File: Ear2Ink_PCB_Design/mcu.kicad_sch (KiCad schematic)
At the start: 43 parts, among them J1 Conn_01x16_Pin, J2 Conn_01x08_Pin, J3 Conn_01x08_Pin, J4 MEM2052-00-195-00-A_REVA, J5 Conn_01x06_Pin, J6 Conn_01x04_Pin, J7 Conn_01x03_Pin, J8 Conn_01x16_Pin, SW1 SW_Push, U1 STM32F411RETx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

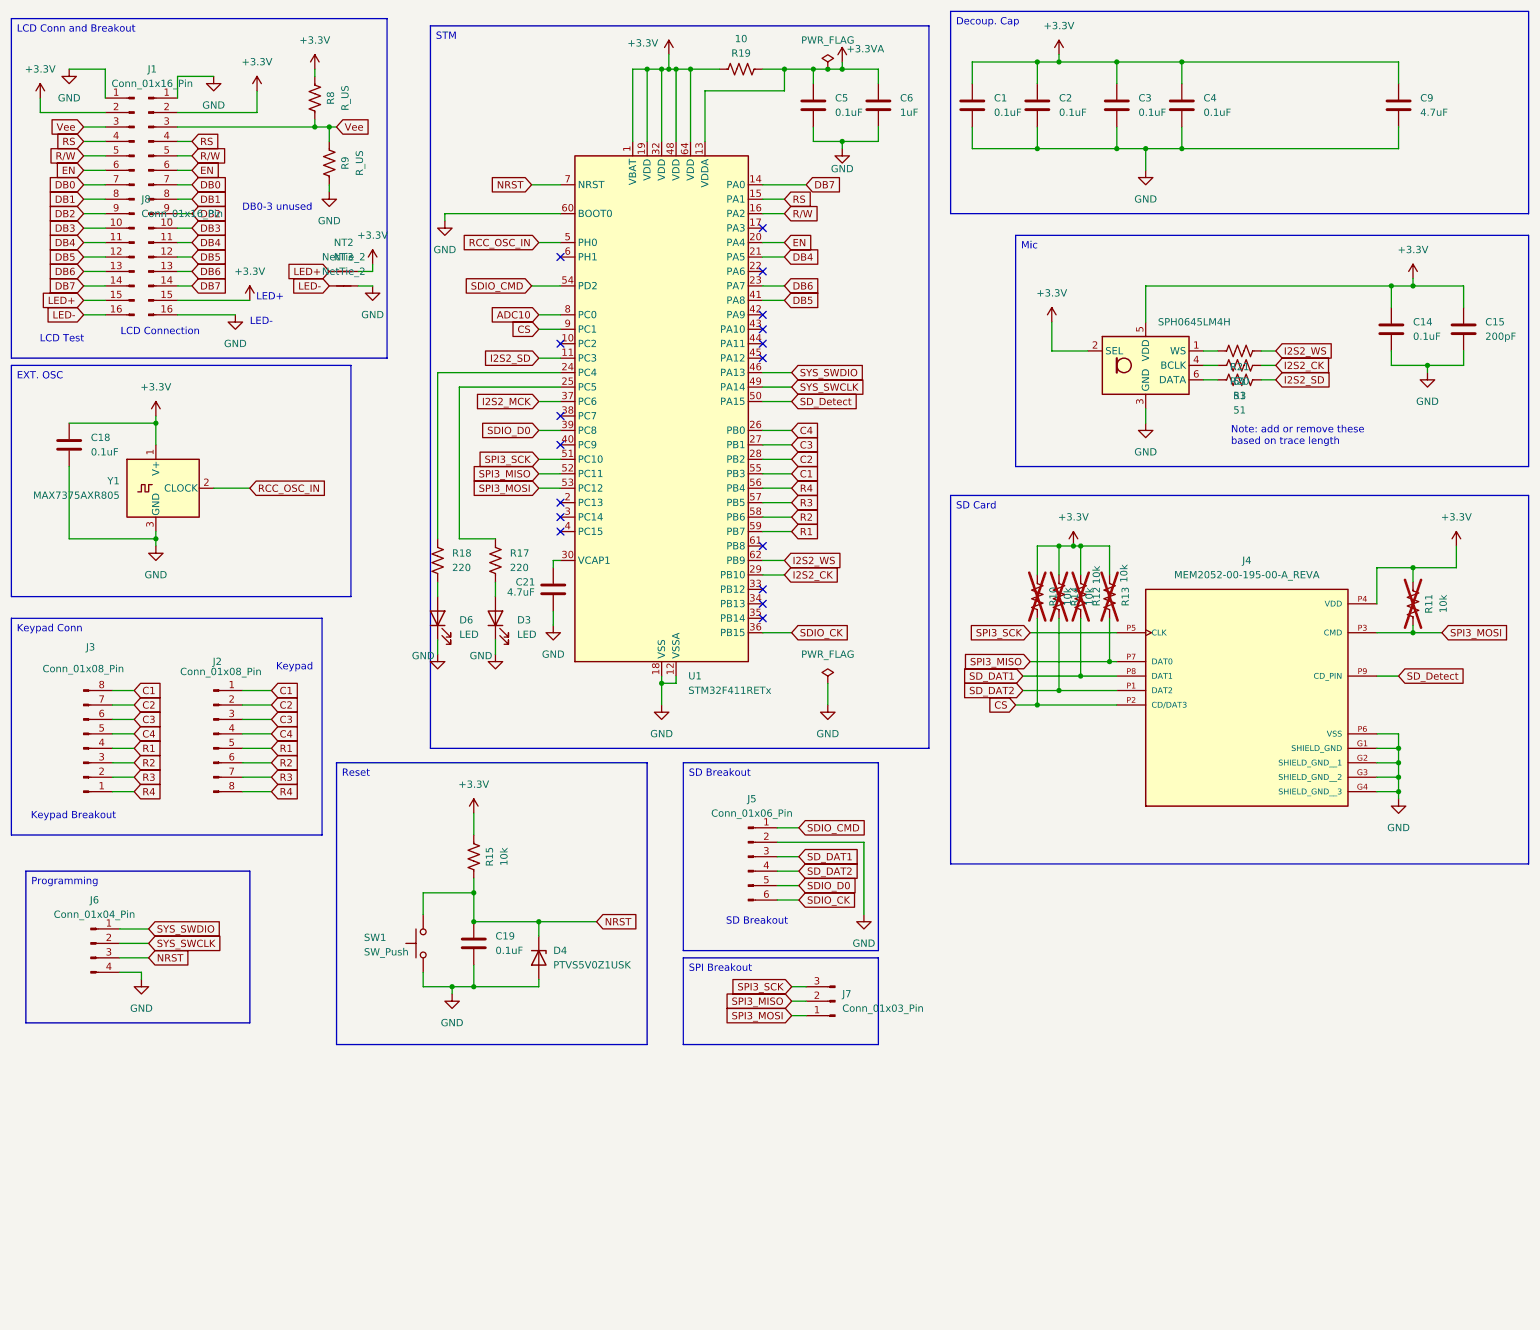
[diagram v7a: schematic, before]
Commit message: New Parts Added
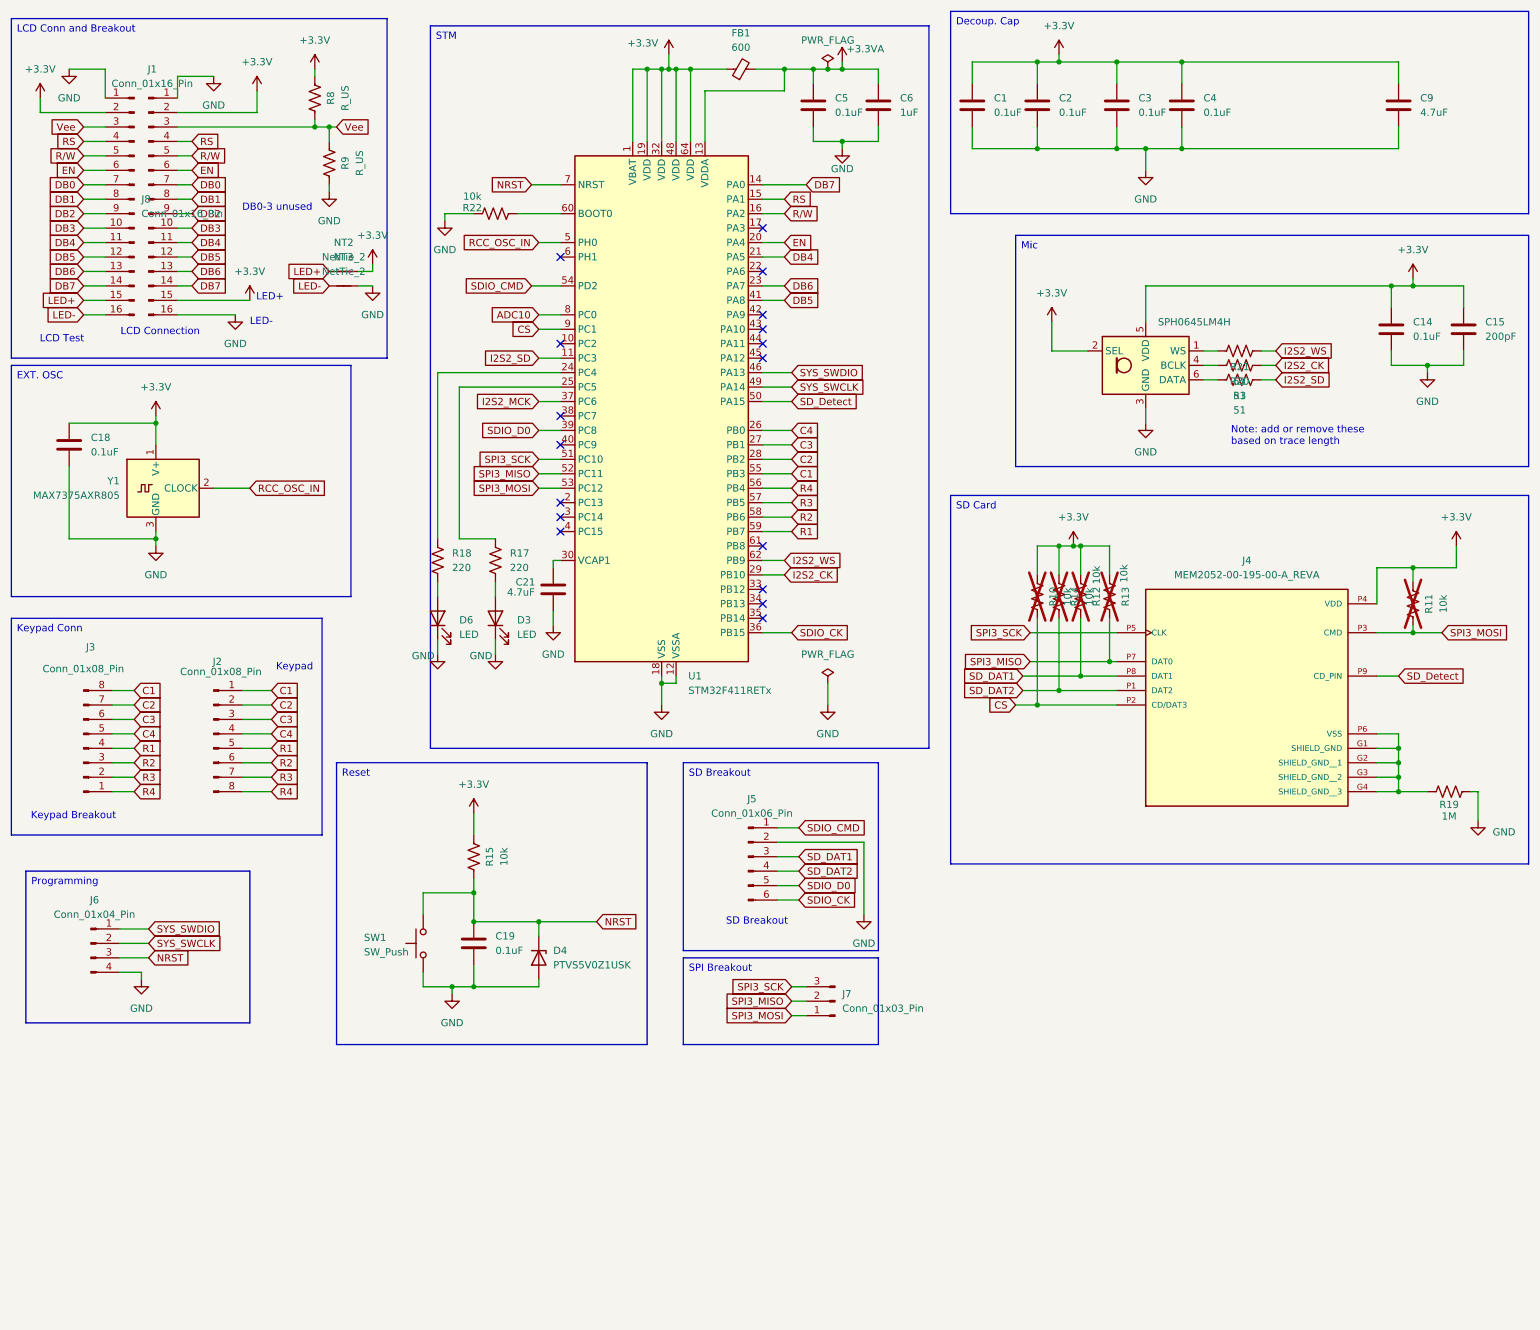
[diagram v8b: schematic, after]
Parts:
- added FB1: 600, symbol Device:FerriteBead_Small
- added R22: 10k, Resistor_SMD:R_0603_1608Metric_Pad0.98x0.95mm_HandSolder, symbol Device:R_US
- R19: value 10 -> 1M
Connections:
- net +3.3V: now also FB1.1; no longer R19.1
- net +3.3VA: now also FB1.2; no longer R19.2
- net GND: now also R19.1, R22.1; no longer J4.G1 (SHIELD_GND), J4.G2 (SHIELD_GND__1), J4.G3 (SHIELD_GND__2), J4.G4 (SHIELD_GND__3), J4.P6 (VSS), U1.60 (BOOT0)
- new net: R22.2, U1.60 (BOOT0)
- new net: J4.G1 (SHIELD_GND), J4.G2 (SHIELD_GND__1), J4.G3 (SHIELD_GND__2), J4.G4 (SHIELD_GND__3), J4.P6 (VSS), R19.2
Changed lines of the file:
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@@
 	)
 	(junction
-		(at 260.35 151.13)
-		(diameter 0)
-		(color 0 0 0 0)
-	)
-	(junction
 		(at 97.79 173.99)
 		(diameter 0)
@@
 	)
 	(junction
+		(at 260.35 151.13)
+		(diameter 0)
+		(color 0 0 0 0)
+	)
+	(junction
 		(at 157.48 24.13)
 		(diameter 0)
@@
 	(wire
 		(pts
+			(xy 260.35 151.13) (xy 265.43 151.13)
+		)
+		(stroke
+			(width 0)
+			(type default)
+		)
+	)
+	(wire
+		(pts
 			(xy 34.29 148.59) (xy 38.1 148.59)
 		)
@@
 	(wire
 		(pts
+			(xy 105.41 49.53) (xy 113.03 49.53)
+		)
+		(stroke
+			(width 0)
+			(type default)
+		)
+	)
+	(wire
+		(pts
 			(xy 152.4 24.13) (xy 157.48 24.13)
 		)
@@
 	(wire
 		(pts
-			(xy 113.03 49.53) (xy 92.71 49.53)
-		)
-		(stroke
-			(width 0)
-			(type default)
-		)
-	)
-	(wire
-		(pts
 			(xy 91.44 114.3) (xy 91.44 116.84)
 		)
@@
 	(wire
 		(pts
-			(xy 148.59 24.13) (xy 152.4 24.13)
-		)
-		(stroke
-			(width 0)
-			(type default)
-		)
-	)
-	(wire
-		(pts
 			(xy 35.56 175.26) (xy 40.64 175.26)
 		)
@@
 	(wire
 		(pts
+			(xy 147.32 24.13) (xy 152.4 24.13)
+		)
+		(stroke
+			(width 0)
+			(type default)
+		)
+	)
+	(wire
+		(pts
 			(xy 109.22 92.71) (xy 113.03 92.71)
 		)
@@
 	(wire
 		(pts
+			(xy 274.32 151.13) (xy 274.32 156.21)
+		)
+		(stroke
+			(width 0)
+			(type default)
+		)
+	)
+	(wire
+		(pts
 			(xy 59.69 27.94) (xy 59.69 31.75)
 		)
@@
 	(wire
 		(pts
-			(xy 260.35 151.13) (xy 260.35 152.4)
+			(xy 273.05 151.13) (xy 274.32 151.13)
 		)
 		(stroke
@@
 	(wire
 		(pts
-			(xy 135.89 24.13) (xy 140.97 24.13)
+			(xy 135.89 24.13) (xy 142.24 24.13)
 		)
 		(stroke
@@
 	(wire
 		(pts
+			(xy 92.71 49.53) (xy 97.79 49.53)
+		)
+		(stroke
+			(width 0)
+			(type default)
+		)
+	)
+	(wire
+		(pts
 			(xy 69.85 33.02) (xy 69.85 34.29)
 		)
@@
 	(symbol
 		(lib_id "Device:R_US")
+		(at 101.6 49.53 90)
+		(unit 1)
+		(exclude_from_sim no)
+		(in_bom yes)
+		(on_board yes)
+		(dnp no)
+		(property "Reference" "R22"
+			(at 97.536 48.514 90)
+			(effects
+				(font
+					(size 1.27 1.27)
+				)
+			)
+		)
+		(property "Value" "10k"
+			(at 97.536 46.482 90)
+			(effects
+				(font
+					(size 1.27 1.27)
+				)
+			)
+		)
+		(property "Footprint" "Resistor_SMD:R_0603_1608Metric_Pad0.98x0.95mm_HandSolder"
+			(at 101.854 48.514 90)
+			(effects
+				(font
+					(size 1.27 1.27)
+				)
+				(hide yes)
+			)
+		)
+		(property "Datasheet" "~"
+			(at 101.6 49.53 0)
+			(effects
+				(font
+					(size 1.27 1.27)
+				)
+				(hide yes)
+			)
+		)
+		(property "Description" "Resistor, US symbol"
+			(at 101.6 49.53 0)
+			(effects
+				(font
+					(size 1.27 1.27)
+				)
+				(hide yes)
+			)
+		)
+		(pin "2"
+		)
+		(pin "1"
+		)
+		(instances
+			(project "Ear2Ink_PCB_Design"
+				(path "/cdb6d8ac-bdfd-4608-bf70-aa82e76498ad/2ddad00a-af62-4659-9017-a3cd158a818d"
+					(reference "R22")
+					(unit 1)
+				)
+			)
+		)
+	)
+	(symbol
+		(lib_id "Device:R_US")
 		(at 232.41 78.74 270)
 		(unit 1)
@@
 	)
 	(symbol
-		(lib_id "Device:R_US")
-		(at 144.78 24.13 90)
-		(unit 1)
-		(exclude_from_sim no)
-		(in_bom yes)
-		(on_board yes)
-		(dnp no)
-		(property "Reference" "R19"
-			(at 144.78 21.336 90)
-			(effects
-				(font
-					(size 1.27 1.27)
-				)
-			)
-		)
-		(property "Value" "10"
-			(at 144.78 18.796 90)
-			(effects
-				(font
-					(size 1.27 1.27)
-				)
-			)
-		)
-		(property "Footprint" "Resistor_SMD:R_0603_1608Metric_Pad0.98x0.95mm_HandSolder"
-			(at 145.034 23.114 90)
-			(effects
-				(font
-					(size 1.27 1.27)
-				)
-				(hide yes)
-			)
-		)
-		(property "Datasheet" "~"
-			(at 144.78 24.13 0)
-			(effects
-				(font
-					(size 1.27 1.27)
-				)
-				(hide yes)
-			)
-		)
-		(property "Description" "Resistor, US symbol"
-			(at 144.78 24.13 0)
-			(effects
-				(font
-					(size 1.27 1.27)
-				)
-				(hide yes)
-			)
-		)
-		(pin "2"
-		)
-		(pin "1"
-		)
-		(instances
-			(project "Ear2Ink_PCB_Design"
-				(path "/cdb6d8ac-bdfd-4608-bf70-aa82e76498ad/2ddad00a-af62-4659-9017-a3cd158a818d"
-					(reference "R19")
-					(unit 1)
-				)
-			)
-		)
-	)
-	(symbol
 		(lib_id "Device:NetTie_2")
 		(at 74.93 59.69 0)
@@
 	)
 	(symbol
+		(lib_id "Device:FerriteBead_Small")
+		(at 144.78 24.13 90)
+		(unit 1)
+		(exclude_from_sim no)
+		(in_bom yes)
+		(on_board yes)
+		(dnp no)
+		(fields_autoplaced yes)
+		(property "Reference" "FB1"
+			(at 144.7419 17.78 90)
+			(effects
+				(font
+					(size 1.27 1.27)
+				)
+			)
+		)
+		(property "Value" "600"
+			(at 144.7419 20.32 90)
+			(effects
+				(font
+					(size 1.27 1.27)
+				)
+			)
+		)
+		(property "Footprint" ""
+			(at 144.78 25.908 90)
+			(effects
+				(font
+					(size 1.27 1.27)
+				)
+				(hide yes)
+			)
+		)
+		(property "Datasheet" "~"
+			(at 144.78 24.13 0)
+			(effects
+				(font
+					(size 1.27 1.27)
+				)
+				(hide yes)
+			)
+		)
+		(property "Description" "Ferrite bead, small symbol"
+			(at 144.78 24.13 0)
+			(effects
+				(font
+					(size 1.27 1.27)
+				)
+				(hide yes)
+			)
+		)
+		(pin "2"
+		)
+		(pin "1"
+		)
+		(instances
+			(project ""
+				(path "/cdb6d8ac-bdfd-4608-bf70-aa82e76498ad/2ddad00a-af62-4659-9017-a3cd158a818d"
+					(reference "FB1")
+					(unit 1)
+				)
+			)
+		)
+	)
+	(symbol
 		(lib_id "Device:C")
 		(at 185.42 30.48 0)
@@
 	)
 	(symbol
+		(lib_id "Device:R_US")
+		(at 269.24 151.13 270)
+		(unit 1)
+		(exclude_from_sim no)
+		(in_bom yes)
+		(on_board yes)
+		(dnp no)
+		(property "Reference" "R19"
+			(at 269.24 153.416 90)
+			(effects
+				(font
+					(size 1.27 1.27)
+				)
+			)
+		)
+		(property "Value" "1M"
+			(at 269.24 155.448 90)
+			(effects
+				(font
+					(size 1.27 1.27)
+				)
+			)
+		)
+		(property "Footprint" "Resistor_SMD:R_0603_1608Metric_Pad0.98x0.95mm_HandSolder"
+			(at 268.986 152.146 90)
+			(effects
+				(font
+					(size 1.27 1.27)
+				)
+				(hide yes)
+			)
+		)
+		(property "Datasheet" "~"
+			(at 269.24 151.13 0)
+			(effects
+				(font
+					(size 1.27 1.27)
+				)
+				(hide yes)
+			)
+		)
+		(property "Description" "Resistor, US symbol"
+			(at 269.24 151.13 0)
+			(effects
+				(font
+					(size 1.27 1.27)
+				)
+				(hide yes)
+			)
+		)
+		(pin "2"
+		)
+		(pin "1"
+		)
+		(instances
+			(project "Ear2Ink_PCB_Design"
+				(path "/cdb6d8ac-bdfd-4608-bf70-aa82e76498ad/2ddad00a-af62-4659-9017-a3cd158a818d"
+					(reference "R19")
+					(unit 1)
+				)
+			)
+		)
+	)
+	(symbol
 		(lib_id "power:GND")
 		(at 52.07 25.4 0)
@@
 	(symbol
 		(lib_id "power:GND")
-		(at 260.35 152.4 0)
+		(at 274.32 156.21 0)
 		(unit 1)
 		(exclude_from_sim no)
@@
 		(on_board yes)
 		(dnp no)
-		(fields_autoplaced yes)
 		(property "Reference" "#PWR029"
-			(at 260.35 158.75 0)
+			(at 274.32 162.56 0)
 			(effects
 				(font
@@
 		)
 		(property "Value" "GND"
-			(at 260.35 157.48 0)
+			(at 278.892 158.242 0)
 			(effects
 				(font
@@
 		)
 		(property "Footprint" ""
-			(at 260.35 152.4 0)
+			(at 274.32 156.21 0)
 			(effects
 				(font
@@
 		)
 		(property "Datasheet" ""
-			(at 260.35 152.4 0)
+			(at 274.32 156.21 0)
 			(effects
 				(font
@@
 		)
 		(property "Description" "Power symbol creates a global label with name \"GND\" , ground"
-			(at 260.35 152.4 0)
+			(at 274.32 156.21 0)
 			(effects
 				(font
